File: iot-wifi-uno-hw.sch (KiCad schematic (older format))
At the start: 56 parts, among them J1 JACK_2P, P1 CONN_01X08, P2 CONN_01X08, P3 CONN_01X06, P4 CONN_01X10, P5 CONN_01X04, Q1 Q_NPN_CBE, Q2 Q_NPN_CBE, SW1 GPIO16, SW2 GPIO0, SW3 REST, U1 usb_mini_b, U2 NCP1117ST33T3G_MountingTab, U3 MCP16311-MS, U4 CH340G, U5 ESP-12E, X1 CRYSTAL_ABM3C

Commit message: add PCB
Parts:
- removed J1: JACK_2P, symbol JACK_2P
- removed SW3: REST, symbol SW_PUSH_Small_Horizontal
- removed U2: NCP1117ST33T3G_MountingTab, TO_SOT_Packages_SMD:SOT-223, symbol NCP1117ST33T3G_MountingTab
- added CON1: BARREL_JACK, Connectors:BARREL_JACK, symbol BARREL_JACK
- added R19: 3K/1%, ESP8266:R_0603, symbol R_Small
- added R20: 1K/1%, ESP8266:R_0603, symbol R_Small
- added U2: BD00GA5WEFJ, ESP8266:HTSOP-J8, symbol BD00GA5WEFJ
- C1: value 10uF/25V -> 1uF/25V; footprint ESP8266:C_0603 -> Capacitors_SMD:C_1210_HandSoldering
- C11, C12, C15, C16: footprint ESP8266:C_0603 -> Capacitors_SMD:C_1210_HandSoldering
- C2: footprint (none) -> ESP8266:C_0603
- C3: value 10uF -> 1uF/25V; footprint ESP8266:C_0603 -> Capacitors_SMD:C_1210_HandSoldering
- C4, C5: value 22pF -> 8pF
- C7: value 10uF -> 10uF/25v; footprint ESP8266:C_0603 -> Capacitors_SMD:C_1210_HandSoldering
- D1, D3: footprint (none) -> LEDs:LED_0603
- D2, D4: footprint (none) -> ESP8266:do214aa
- L1: footprint (none) -> Choke_SMD:Choke_SMD_Wuerth-WE-PD2-Typ-MS
- Q1, Q2: footprint (none) -> TO_SOT_Packages_SMD:SOT-323
- SW1: value GPIO16 -> REST; footprint (none) -> Buttons_Switches_SMD:SW_SPST_FSMSM
- SW2: footprint (none) -> Buttons_Switches_SMD:SW_SPST_FSMSM
- U3: footprint Housings_SSOP:MSOP-8_3x3mm_Pitch0.65mm -> Housings_SSOP:MSOP-8-1EP_3x3mm_Pitch0.65mm
- U4: footprint SOIC-16_N -> Housings_SOIC:SOIC-16_3.9x9.9mm_Pitch1.27mm
- X1: footprint (none) -> ESP8266:Crystal_SMD_3225_4Pads
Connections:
- net +3V3: now also P5.1 (P1), R19.1, U2.1 (VO); no longer P5.2 (P2)
- net +5V: now also U2.5 (EN), U2.8 (VCC)
- net GND: now also P5.2 (P2), CON1.2, CON1.3, R20.2, U2.3 (GND), U2.9 (FIN); no longer P5.1 (P1), U1.7 (GND), U1.8 (GND), U1.9 (GND), U4.8 (XO)
- net GPIO09: now also P3.4 (P4)
- net XO: now reaches C4.1, X1.1
- net XO: now also U4.8 (XO)
- net at D4.2 (A): now also CON1.1
- new net: R19.2, R20.1, U2.2 (FB)
- no-connect marks 20 -> 26
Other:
- note removed: "A3"
- moved on the sheet: D1, R8

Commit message: add VIN
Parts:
- added C17: 100nF, ESP8266:C_0603, symbol C_Small
- added R21, R22: 10k, ESP8266:R_0603, symbol R_Small
- added U6: MCP6002, symbol MCP6002
- added U7: MOSFET-P, TO_SOT_Packages_SMD:SOT-23_Handsoldering, symbol MOSFET-P
- D2: value N5819/SS14/S4(SOD_323) -> ss24
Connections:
- net +3V3: now also U6.2 (-)
- net +5V: now also C17.1, U6.8 (V+), U7.2
- net GND: now also C17.2, R22.1, U6.4 (V-)
- net VCC: now also U7.3
- net Vin: now reaches P2.8 (P8)
- net Vin: now also C11.1, C12.1, D4.1 (K), U3.3 (EN), U3.4 (Vin), R21.2
- new net: U6.1, U7.1
- new net: R21.1, R22.2, U6.3 (+)
- no-connect marks 26 -> 25
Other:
- moved on the sheet: C11, C12, C13, C14, C15, C16, CON1, D2, D4, L1, R15, R16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

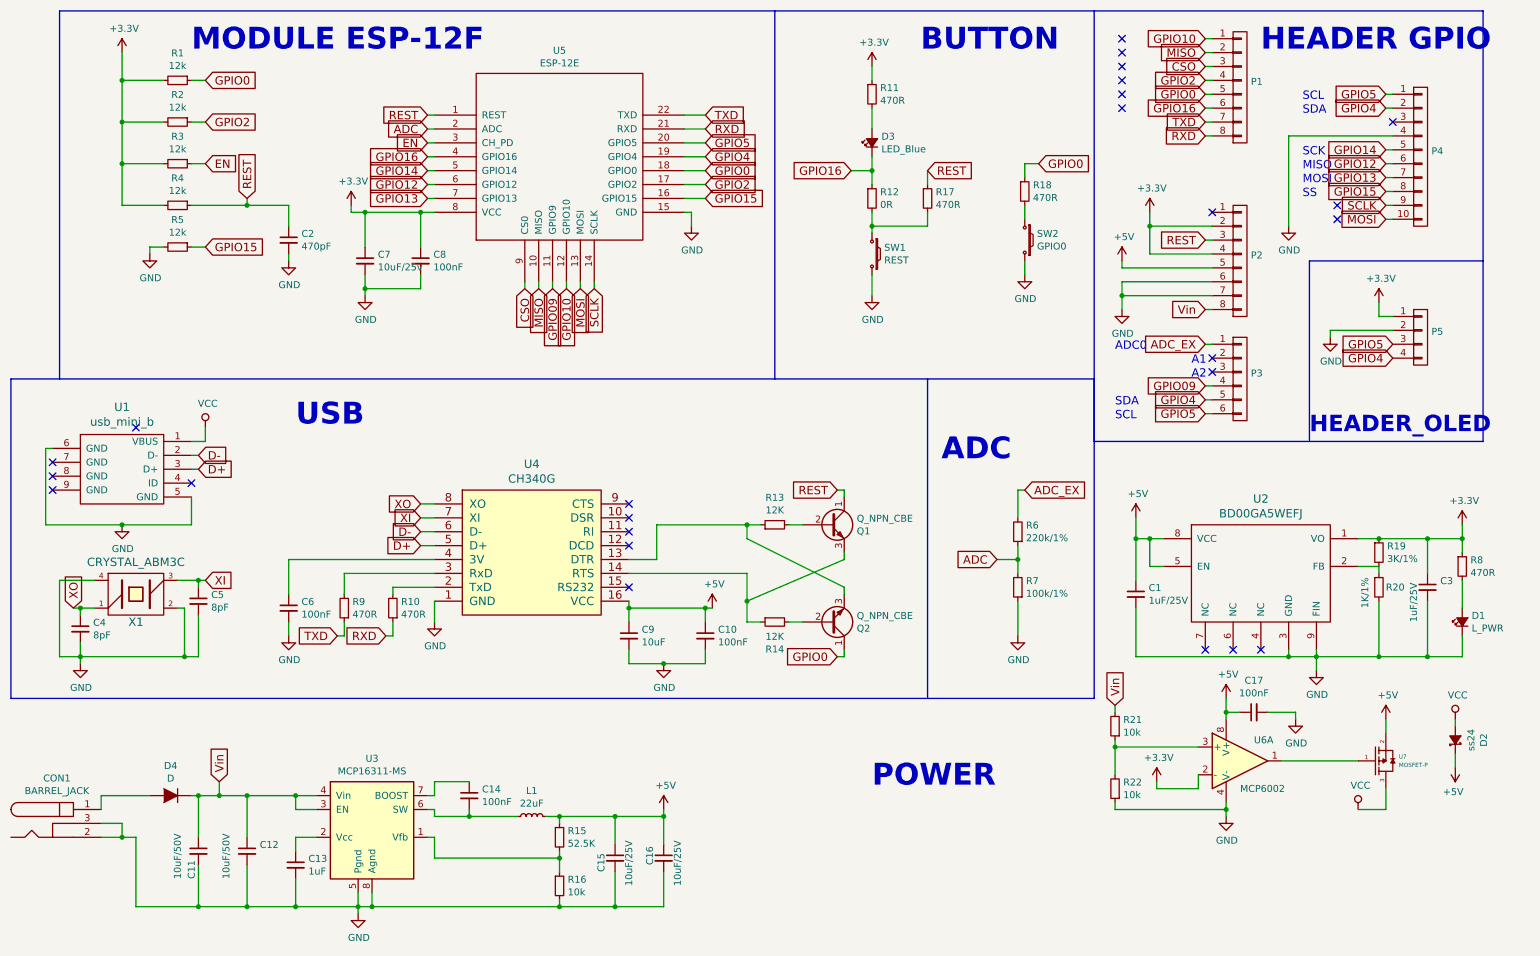
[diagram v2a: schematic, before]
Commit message: add VIN to PCB - MOSFET & OpAmp
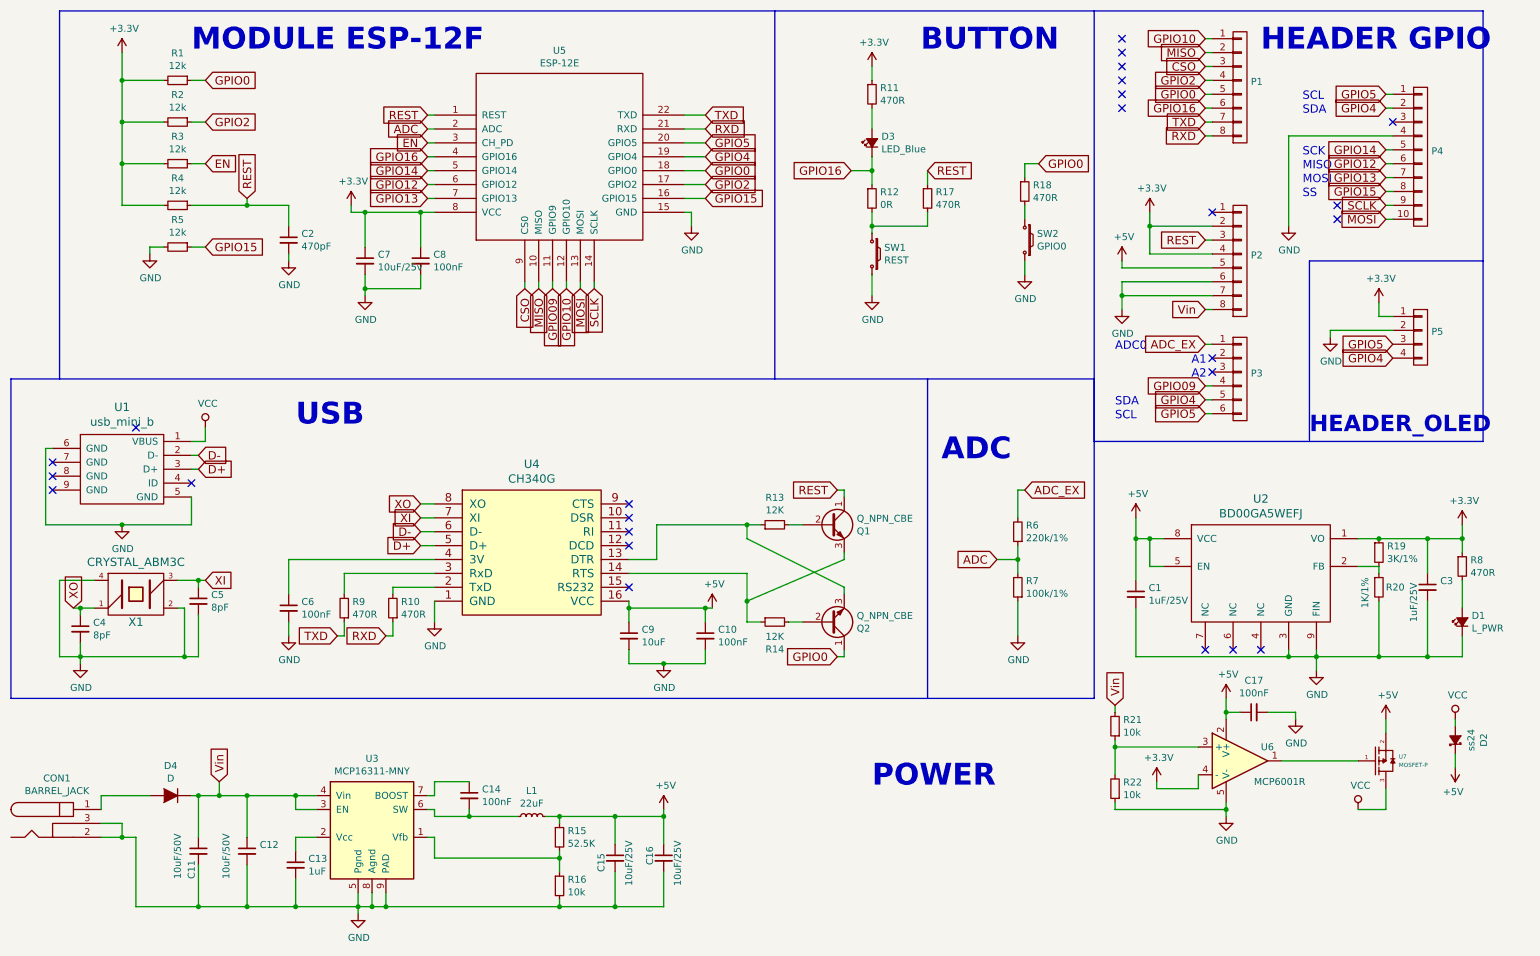
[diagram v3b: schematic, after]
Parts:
- removed U3: MCP16311-MS, Housings_SSOP:MSOP-8-1EP_3x3mm_Pitch0.65mm, symbol MCP16311-MS
- removed U6: MCP6002, symbol MCP6002
- added U3: MCP16311-MNY, Housings_DFN_QFN:DFN-8-1EP_3x2mm_Pitch0.5mm, symbol MCP16311-MNY
- added U6: MCP6001R, TO_SOT_Packages_SMD:SOT-23-5, symbol MCP6001R
- C7: footprint Capacitors_SMD:C_1210_HandSoldering -> ESP8266:C_0603
- U7: footprint TO_SOT_Packages_SMD:SOT-23_Handsoldering -> TO_SOT_Packages_SMD:SOT-23
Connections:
- net +3V3: now also U6.4 (-)
- net +5V: now also U6.2 (V+)
- net GND: now also U3.5 (Pgnd), U3.8 (Agnd), U3.9 (PAD), U6.5 (V-)
- net Vin: now also U3.3 (EN), U3.4 (Vin)
- net at R15.2, R16.1: now also U3.1 (Vfb)
- net at C13.1: now also U3.2 (Vcc)
- net at C14.2, L1.1: now also U3.6 (SW)
- net at C14.1: now also U3.7 (BOOST)
- net at U7.1: now also U6.1
- net at R21.1, R22.2: now also U6.3 (+)

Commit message: Completed PCB
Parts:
- GPIO0: renamed from SW2; footprint Buttons_Switches_SMD:SW_SPST_FSMSM -> ESP8266:Tact_Switch_TS6X3.6
- RST1: renamed from SW1; footprint Buttons_Switches_SMD:SW_SPST_FSMSM -> ESP8266:Tact_Switch_TS6X3.6
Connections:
- net +3V3: no longer P2.2 (P2)
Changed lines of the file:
@@
 $EndComp
 $Comp
-L SW_PUSH_Small_Horizontal SW1
+L SW_PUSH_Small_Horizontal RST1
 U 1 1 58270826
 P 6700 2250
-F 0 "SW1" V 6654 2338 50  0000 L CNN
+F 0 "RST1" V 6654 2338 50  0000 L CNN
 F 1 "REST" V 6745 2338 50  0000 L CNN
-F 2 "Buttons_Switches_SMD:SW_SPST_FSMSM" H 6700 2450 50  0001 C CNN
+F 2 "ESP8266:Tact_Switch_TS6X3.6" H 6700 2450 50  0001 C CNN
 F 3 "" H 6700 2450 50  0000 C CNN
 	1    6700 2250
@@
 $EndComp
 $Comp
-L SW_PUSH_Small_Horizontal SW2
+L SW_PUSH_Small_Horizontal GPIO0
 U 1 1 5827B946
 P 7800 2150
-F 0 "SW2" V 7754 2238 50  0000 L CNN
+F 0 "GPIO0" V 7754 2238 50  0000 L CNN
 F 1 "GPIO0" V 7845 2238 50  0000 L CNN
-F 2 "Buttons_Switches_SMD:SW_SPST_FSMSM" H 7800 2350 50  0001 C CNN
+F 2 "ESP8266:Tact_Switch_TS6X3.6" H 7800 2350 50  0001 C CNN
 F 3 "" H 7800 2350 50  0000 C CNN
 	1    7800 2150
@@
 Text Notes 8450 2950 0    60   ~ 0
 ADC0
-Wire Wire Line
-	9150 2050 8700 2050
-Connection ~ 8700 2050
 Text GLabel 9100 900  0    60   Input ~ 0
 CSO

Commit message: completed PCB
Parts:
- L1: value 22uF -> 22uH
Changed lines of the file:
@@
 P 4250 6300
 F 0 "L1" V 4435 6300 50  0000 C CNN
-F 1 "22uF" V 4344 6300 50  0000 C CNN
+F 1 "22uH" V 4344 6300 50  0000 C CNN
 F 2 "Choke_SMD:Choke_SMD_Wuerth-WE-PD2-Typ-MS" H 4250 6300 50  0001 C CNN
 F 3 "" H 4250 6300 50  0000 C CNN

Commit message: New PCB (#9)
* fix via beetwen U3 & R16

* Delete fp-lib-table

* deleted iot-wifi-uno-hw-cache.lib

* Fix crystall of CH340G

* modify some track

* Modify footprint MCP16311, add zener to ADC, fix footprint 2 transistor
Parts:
- removed C7: 10uF/25v, ESP8266:C_0603, symbol C_Small
- removed C9: 10uF, ESP8266:C_0603, symbol C_Small
- removed D4: D, ESP8266:do214aa, symbol D
- added D1: SS24, ESP8266:do214aa, symbol D_Schottky_Small
- added D5: ZENER_3.3V, ESP8266:SOD-80, symbol ZENER_Small
- C1: renamed from C4; value 8pF -> 22pF
- C15: renamed from C3; footprint Capacitors_SMD:C_1210_HandSoldering -> ESP8266:C_0603
- C2: renamed from C5; value 8pF -> 22pF
- D3: renamed from D2; value ss24 -> SS24
- Q1, Q2: value Q_NPN_CBE -> MMBT8050LT1G; footprint TO_SOT_Packages_SMD:SOT-323 -> TO_SOT_Packages_SMD:SOT-23
- R10: renamed from R13; value 12K -> 10K
- R11: renamed from R14; value 12K -> 10K
- U7: value MOSFET-P -> IRLM6402
- renumbered C15 to C10, C16 to C11, C10 to C12, C1 to C13, C17 to C14, C11 to C3, C12 to C4, C2 to C5, C13 to C7, C14 to C9, D3 to D2, D1 to D4, GPIO0 to GPIO1, R11 to R12, R12 to R13, R17 to R14, R6 to R15, R7 to R16, R18 to R17, R21 to R18, R22 to R19, R19 to R20, R20 to R21, R8 to R22, R9 to R6, R10 to R7, R15 to R8, R16 to R9, U3 to U2, U4 to U3, U5 to U4, U6 to U5, U2 to U6
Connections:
- wire segments 230 -> 226

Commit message: correct zener placement
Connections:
- wire segments 226 -> 229
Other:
- moved on the sheet: R15, R16
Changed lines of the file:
@@
 LIBS:open-project
 LIBS:MOSFET-P
-LIBS:iot-wifi-uno-hw-cache
 EELAYER 25 0
 EELAYER END
@@
 L R_Small R15
 U 1 1 5827352C
-P 7750 4250
-F 0 "R15" H 7691 4204 50  0000 R CNN
-F 1 "220k/1%" H 7691 4295 50  0000 R CNN
-F 2 "ESP8266:R_0603" H 7750 4250 50  0001 C CNN
-F 3 "" H 7750 4250 50  0000 C CNN
-	1    7750 4250
+P 7530 4240
+F 0 "R15" H 7471 4194 50  0000 R CNN
+F 1 "220k/1%" H 7471 4285 50  0000 R CNN
+F 2 "ESP8266:R_0603" H 7530 4240 50  0001 C CNN
+F 3 "" H 7530 4240 50  0000 C CNN
+	1    7530 4240
 	-1   0    0    1
 $EndComp
@@
 L R_Small R16
 U 1 1 582735DB
-P 7750 4650
-F 0 "R16" H 7691 4604 50  0000 R CNN
-F 1 "100k/1%" H 7691 4695 50  0000 R CNN
-F 2 "ESP8266:R_0603" H 7750 4650 50  0001 C CNN
-F 3 "" H 7750 4650 50  0000 C CNN
-	1    7750 4650
+P 7530 4640
+F 0 "R16" H 7471 4594 50  0000 R CNN
+F 1 "100k/1%" H 7471 4685 50  0000 R CNN
+F 2 "ESP8266:R_0603" H 7530 4640 50  0001 C CNN
+F 3 "" H 7530 4640 50  0000 C CNN
+	1    7530 4640
 	-1   0    0    1
 $EndComp
@@
 L GND #PWR013
 U 1 1 5827364E
-P 7750 5000
-F 0 "#PWR013" H 7750 4750 50  0001 C CNN
-F 1 "GND" H 7755 4827 50  0000 C CNN
-F 2 "" H 7750 5000 50  0000 C CNN
-F 3 "" H 7750 5000 50  0000 C CNN
-	1    7750 5000
-	1    0    0    -1
-$EndComp
-Text GLabel 7600 4450 0    60   Input ~ 0
+P 7530 4990
+F 0 "#PWR013" H 7530 4740 50  0001 C CNN
+F 1 "GND" H 7535 4817 50  0000 C CNN
+F 2 "" H 7530 4990 50  0000 C CNN
+F 3 "" H 7530 4990 50  0000 C CNN
+	1    7530 4990
+	1    0    0    -1
+$EndComp
+Text GLabel 7380 4440 0    60   Input ~ 0
 ADC
 Text GLabel 7850 3550 2    60   Input ~ 0
@@
 NoConn ~ 9150 3000
 NoConn ~ 9150 3100
-Text Notes 7200 3750 0    157  ~ 31
+Text Notes 7160 3430 0    157  ~ 31
 ADC\n
 Text Notes 2550 3500 0    157  ~ 31
@@
 	3550 4450 2500 4450
 Wire Wire Line
-	7750 3900 7750 4150
-Connection ~ 7750 4450
-Wire Wire Line
-	7600 4450 7750 4450
-Wire Wire Line
-	7750 4750 7750 5000
-Wire Wire Line
-	7750 4350 7750 4550
+	7970 4840 7970 4580
+Connection ~ 7530 4440
+Wire Wire Line
+	7380 4440 7530 4440
+Wire Wire Line
+	7530 4740 7530 4990
+Wire Wire Line
+	7530 4340 7530 4540
 Wire Wire Line
 	10900 5600 10900 5650
@@
 L ZENER_Small D5
 U 1 1 583437A6
-P 7750 3800
-F 0 "D5" V 7704 3869 50  0000 L CNN
-F 1 "ZENER_3.3V" V 7795 3869 50  0000 L CNN
-F 2 "ESP8266:SOD-80" H 7750 3800 50  0001 C CNN
-F 3 "" H 7750 3800 50  0000 C CNN
-	1    7750 3800
+P 7970 4480
+F 0 "D5" V 7924 4549 50  0000 L CNN
+F 1 "ZENER_3.3V" H 8015 4549 50  0000 L CNN
+F 2 "ESP8266:SOD-80" H 7970 4480 50  0001 C CNN
+F 3 "" H 7970 4480 50  0000 C CNN
+	1    7970 4480
 	0    1    1    0
 $EndComp
 Wire Wire Line
-	7850 3550 7750 3550
-Wire Wire Line
-	7750 3550 7750 3700
+	7530 3550 7530 4140
+Wire Wire Line
+	7530 4840 7970 4840
+Connection ~ 7530 4840
+Wire Wire Line
+	7970 4380 7970 3920
+Wire Wire Line
+	7970 3920 7530 3920
+Connection ~ 7530 3920
+Wire Wire Line
+	7850 3550 7530 3550
 $EndSCHEMATC
